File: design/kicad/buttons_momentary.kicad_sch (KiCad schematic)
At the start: 6 parts, among them SW1 MIDI_Switch_Pushbutton_PV0H24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, SW2 MIDI_Switch_Pushbutton_PV0H24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, SW3 MIDI_Switch_Pushbutton_PV0H24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, SW4 MIDI_Switch_Pushbutton_PV0H24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, SW5 MIDI_Switch_Pushbutton_PV0H24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, SW6 MIDI_Switch_Pushbutton_PV0H24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

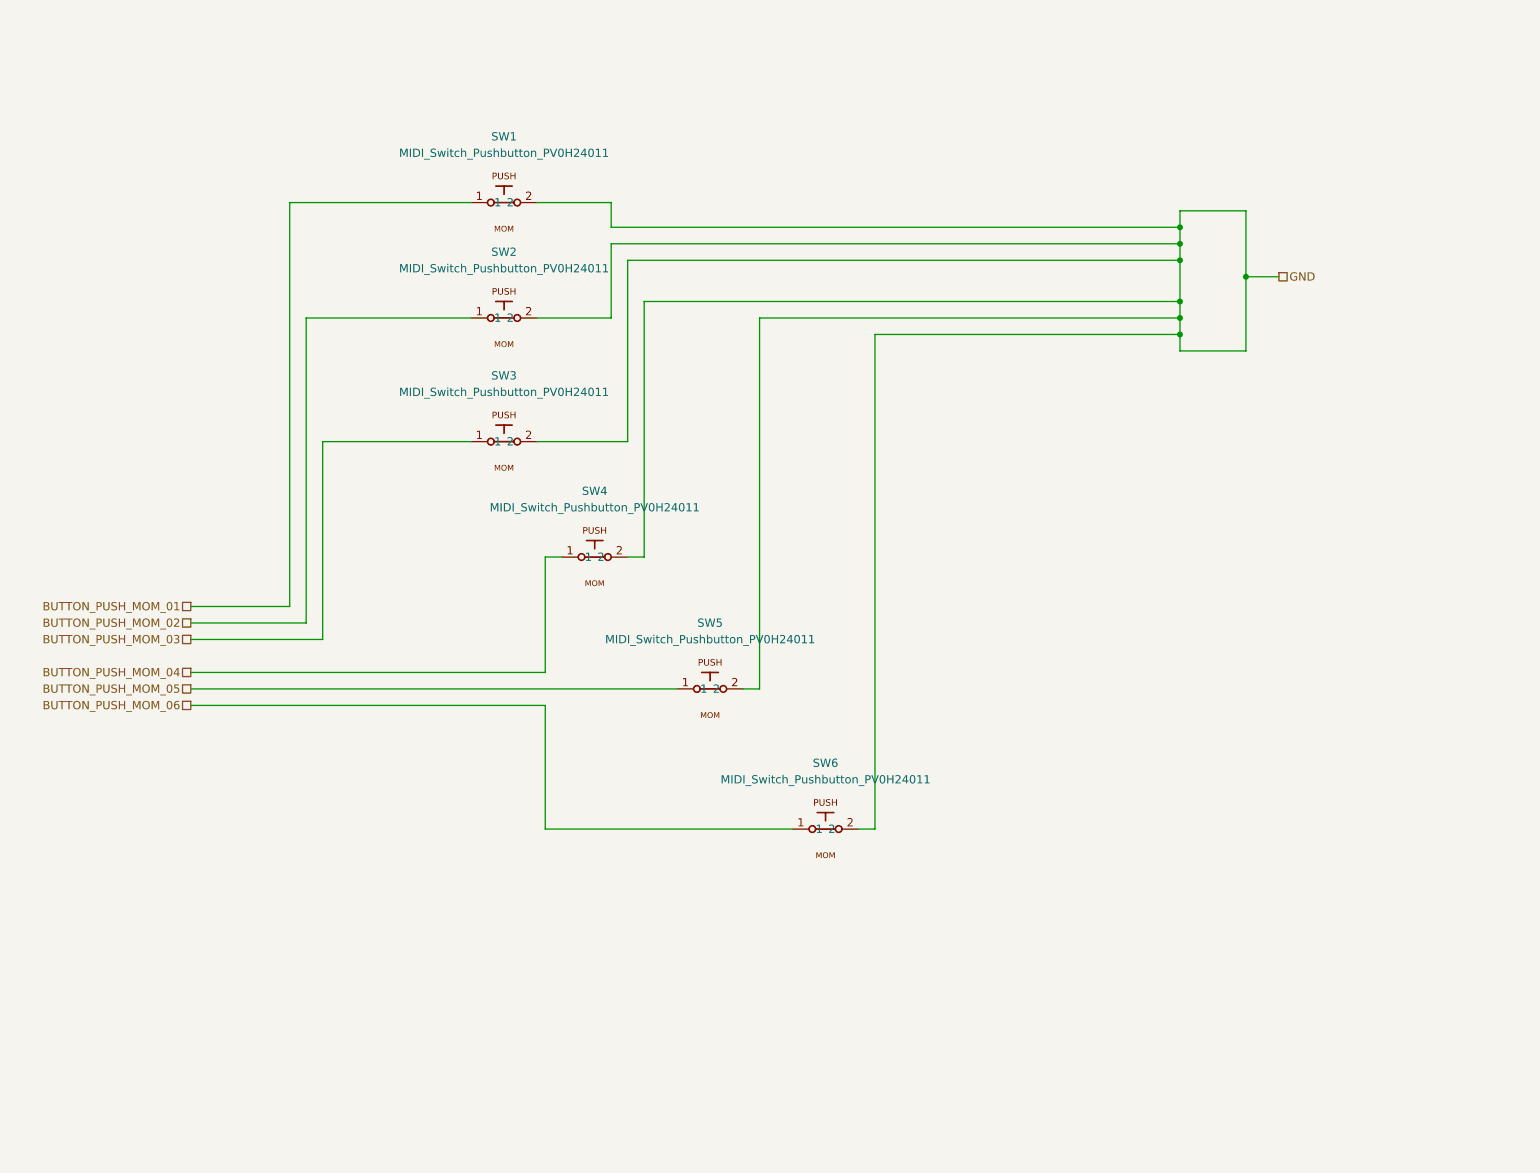
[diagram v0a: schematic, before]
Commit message: Update kicad binary files
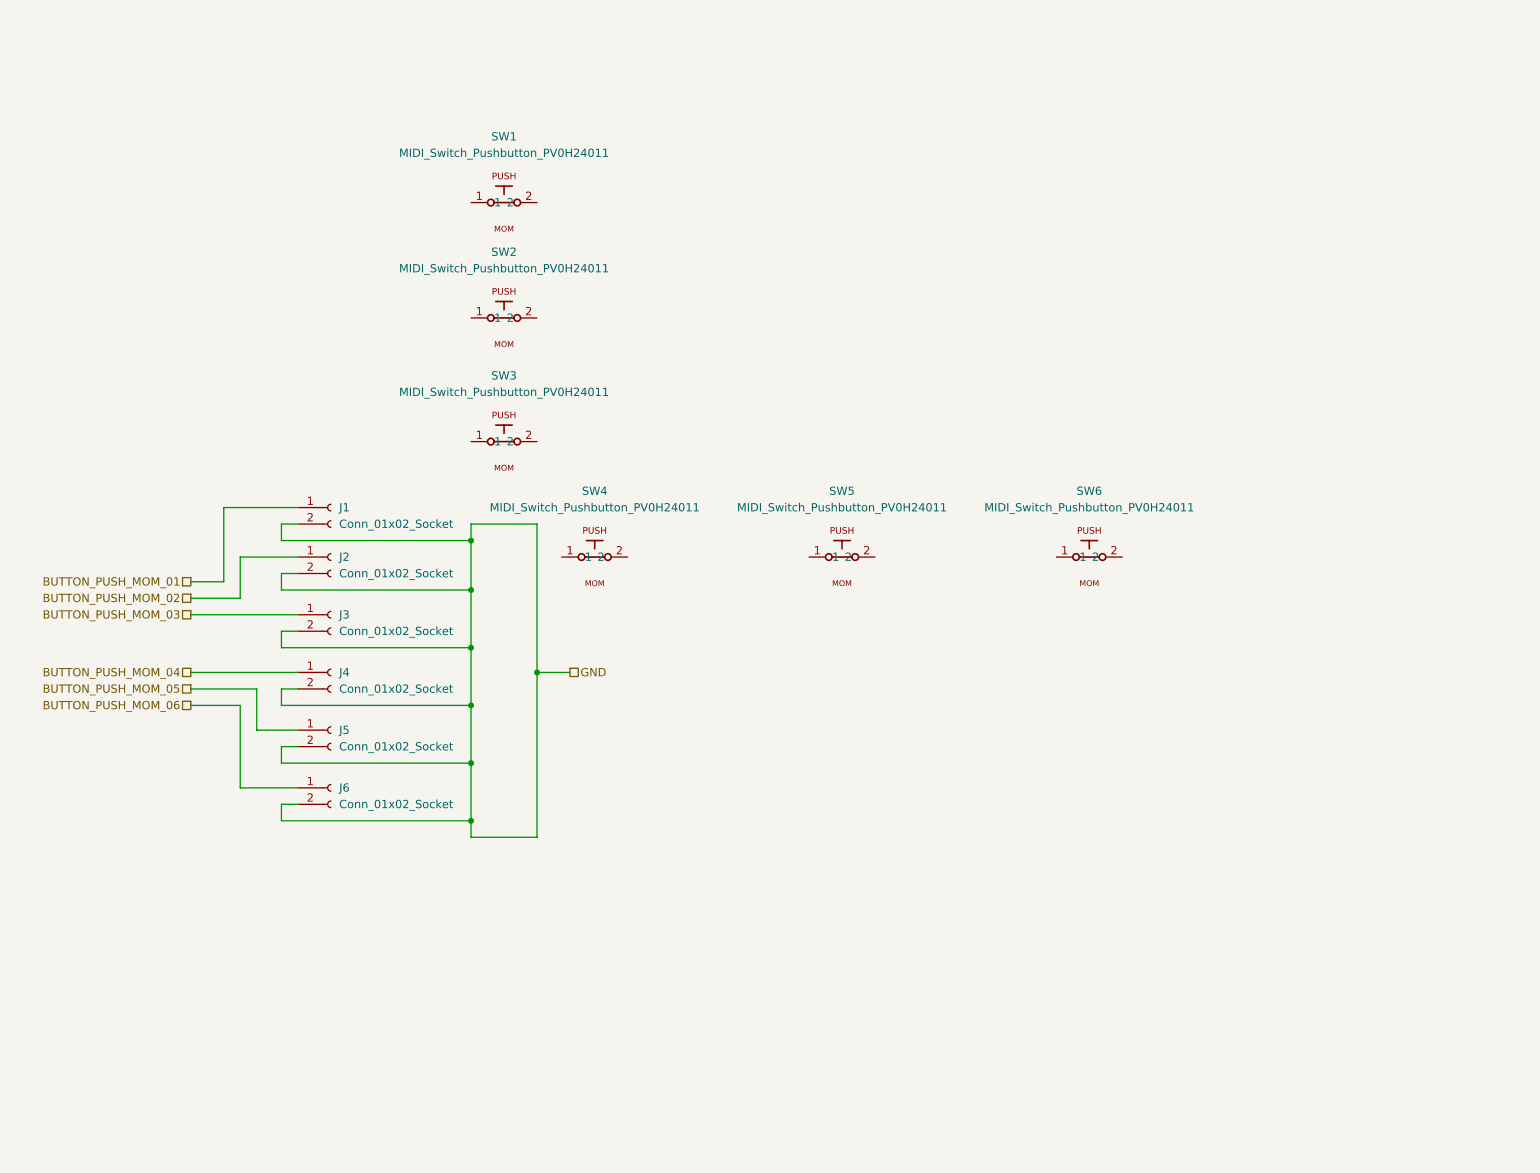
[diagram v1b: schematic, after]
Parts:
- added J1, J2, J3, J4, J5, J6: Conn_01x02_Socket, Connector_JST:JST_XH_B2B-XH-A_1x02_P2.50mm_Vertical, symbol Connector:Conn_01x02_Socket
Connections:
- net BUTTON_PUSH_MOM_01: now also J1.1 (Pin_1); no longer SW1.1
- net BUTTON_PUSH_MOM_02: now also J2.1 (Pin_1); no longer SW2.1
- net BUTTON_PUSH_MOM_03: now also J3.1 (Pin_1); no longer SW3.1
- net BUTTON_PUSH_MOM_04: now also J4.1 (Pin_1); no longer SW4.1
- net BUTTON_PUSH_MOM_05: now also J5.1 (Pin_1); no longer SW5.1
- net BUTTON_PUSH_MOM_06: now also J6.1 (Pin_1); no longer SW6.1
- net GND: now also J1.2 (Pin_2), J2.2 (Pin_2), J3.2 (Pin_2), J4.2 (Pin_2), J5.2 (Pin_2), J6.2 (Pin_2); no longer SW1.2, SW2.2, SW3.2, SW4.2, SW5.2, SW6.2
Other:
- moved on the sheet: SW5, SW6

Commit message: Fix hardware pin configuration and rotary encoder parameters
- Updated CS_PIN from 30 to 28 in SystemConstants.hpp to reflect the correct hardware setup for ILI9341.
- Modified rotary encoder parameters in ConfigurationFactory.cpp, changing the first parameter of asRotaryEncoder from 28 to 23 for proper functionality.
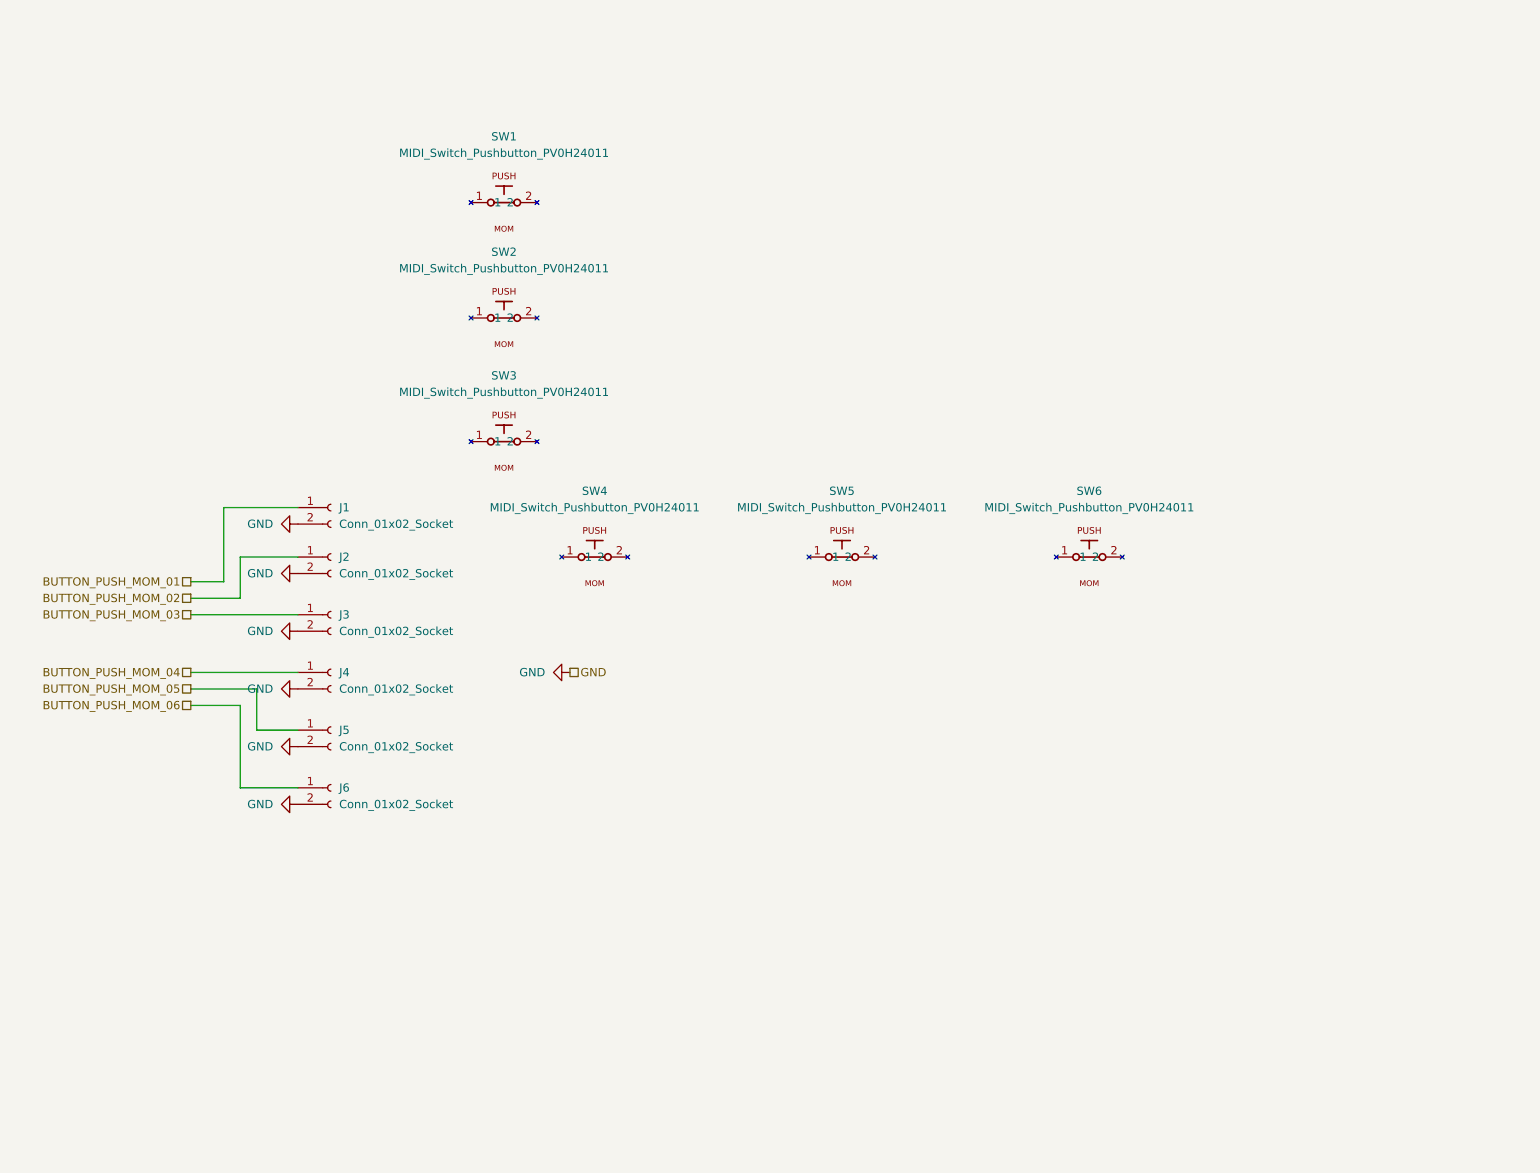
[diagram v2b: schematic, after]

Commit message: Refactor code structure for improved readability and maintainability
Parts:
- SW1, SW2, SW3, SW4, SW5, SW6: value MIDI_Switch_Pushbutton_PV0H24011 -> ~

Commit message: Refactor code structure for improved readability and maintainability
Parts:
- added D31, D32, D33, D34, D35, D36: PESD5V0L1BA,115, KiCad:SOD2512X110N, symbol PESD5V0L1BA_115:PESD5V0L1BA,115
- renumbered J1 to J2, J2 to J3, J3 to J4, J4 to J5, J5 to J6, J6 to J7
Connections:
- net BUTTON_PUSH_MOM_01: now also D31.1 (K1)
- net BUTTON_PUSH_MOM_02: now also D32.1 (K1)
- net BUTTON_PUSH_MOM_03: now also D33.1 (K1)
- net BUTTON_PUSH_MOM_04: now also D34.1 (K1)
- net BUTTON_PUSH_MOM_05: now also D35.1 (K1)
- net BUTTON_PUSH_MOM_06: now also D36.1 (K1)
- net GND: now also D31.2 (K2), D32.2 (K2), D33.2 (K2), D34.2 (K2), D35.2 (K2), D36.2 (K2)
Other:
- moved on the sheet: J2, J3, J4, J5, J6, J7

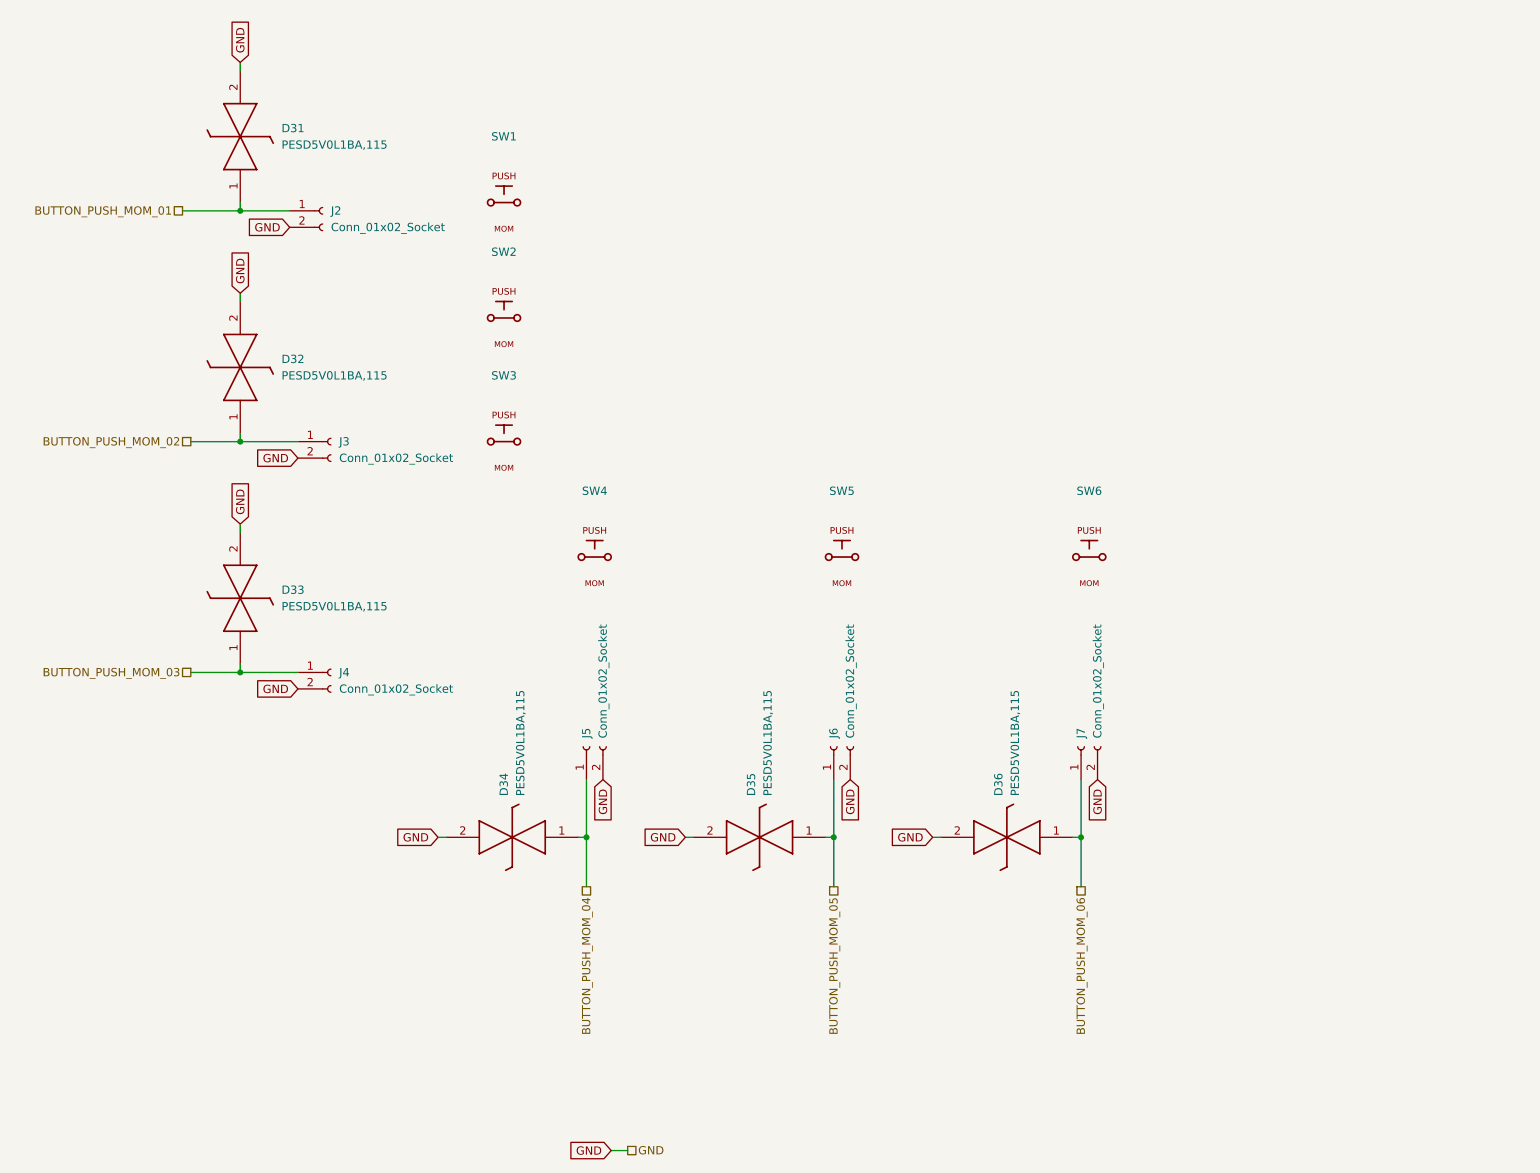
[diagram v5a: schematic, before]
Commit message: Add schematic for MIDI Display MSP2807 with associated components
- Created a new schematic file for the MIDI Display MSP2807.
- Included a unpolarized capacitor (C2) with a value of 100nF.
- Added properties such as reference, value, footprint, and datasheet for the capacitor.
- Integrated the MIDI Display module with detailed pin configurations and properties.
- Defined hierarchical labels for power and data connections (VCC, GND, CS, RST, DC, etc.).
- Ensured all components are marked for BOM inclusion and simulation.
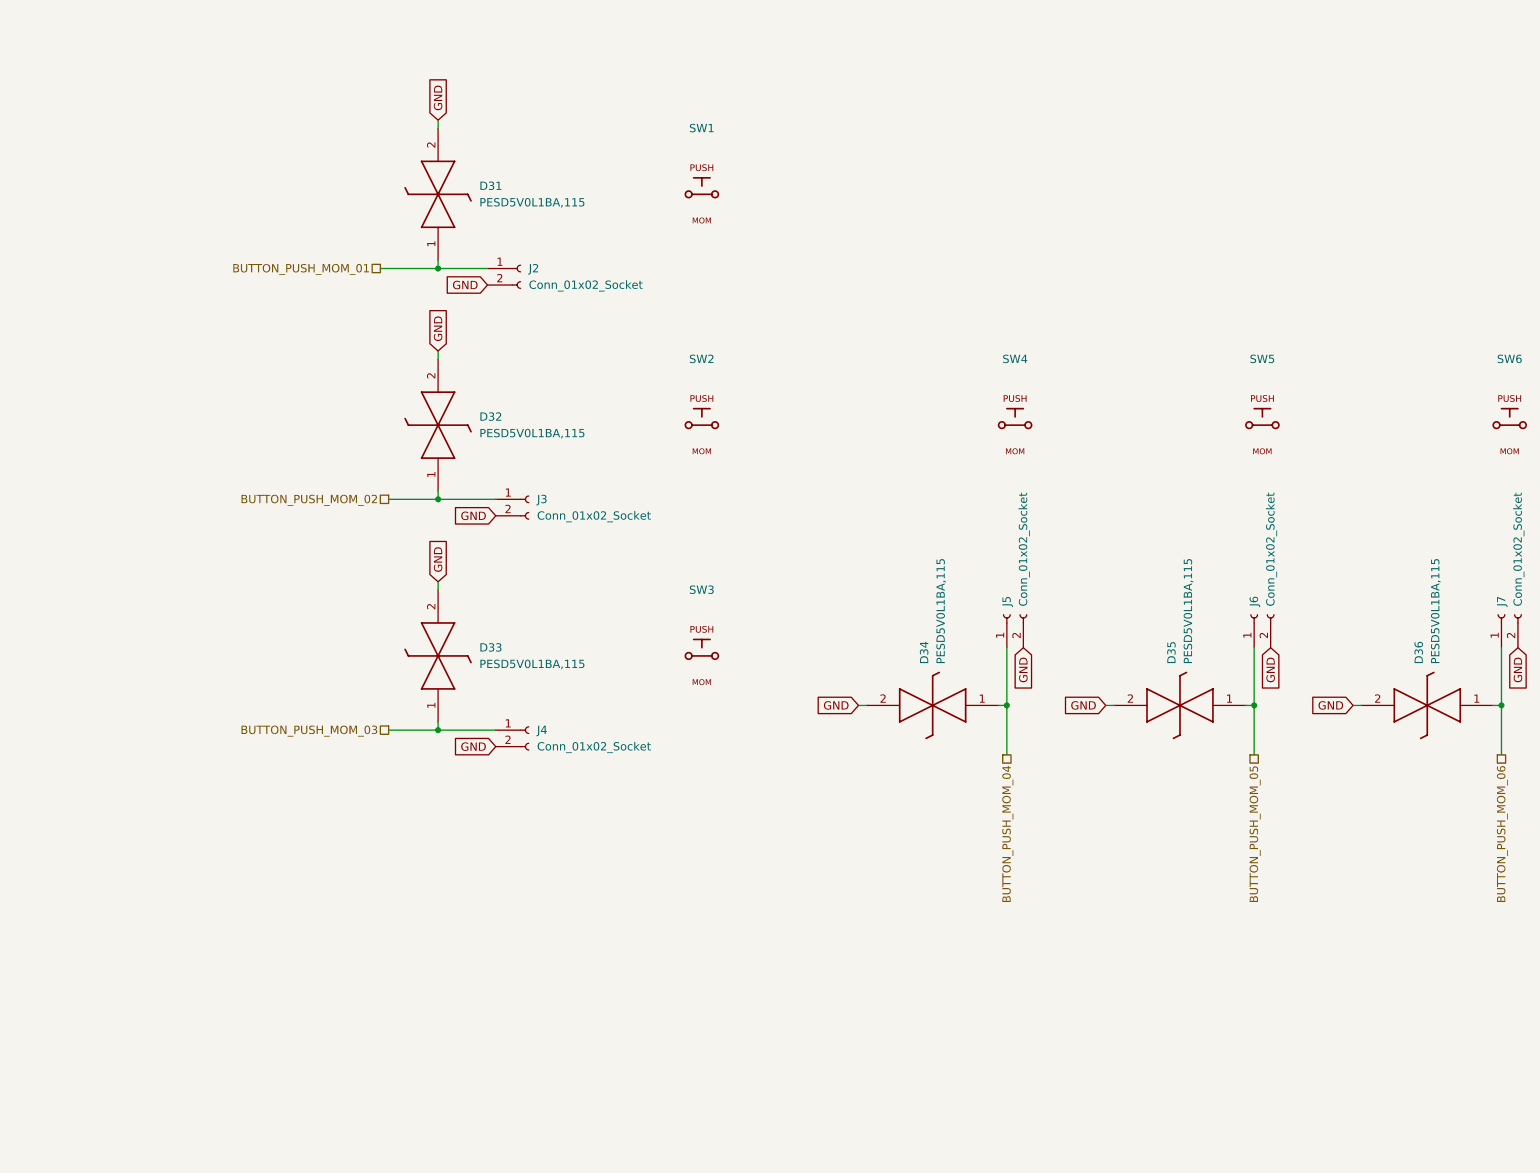
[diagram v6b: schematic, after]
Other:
- moved on the sheet: D31, D32, D33, D34, D35, D36, J2, J3, J4, J5, J6, J7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
